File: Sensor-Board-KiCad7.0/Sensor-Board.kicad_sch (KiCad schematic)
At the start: 73 parts, among them J1 B4B-XH-A, U1 OPA396DCKT, U10 BME680, U13 TCA9548AMRGER, U14 OPA396DCKT, U19 MMBFJ177LT1, U2 OPA396DCKT, U20 MMBFJ177LT1, U21 OPA396DCKT, U22 OPA396DCKT, U25 NAU7802SGI, U26 MMBFJ177LT1, U3 OPA396DCKT, U4 NAU7802SGI

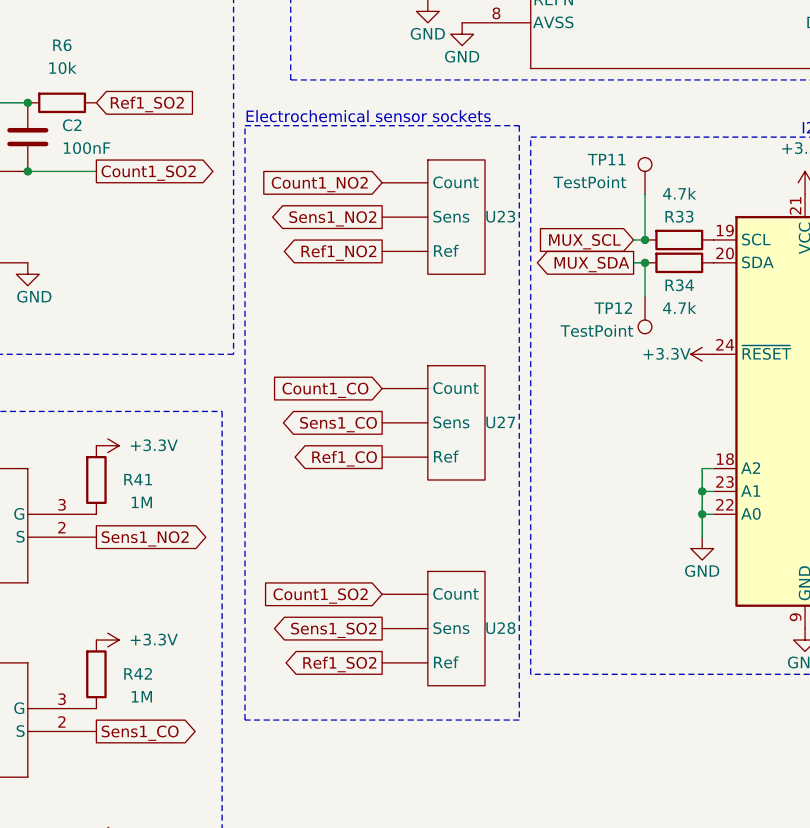
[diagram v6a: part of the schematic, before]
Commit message: Fixed I2C Connector pin numbers
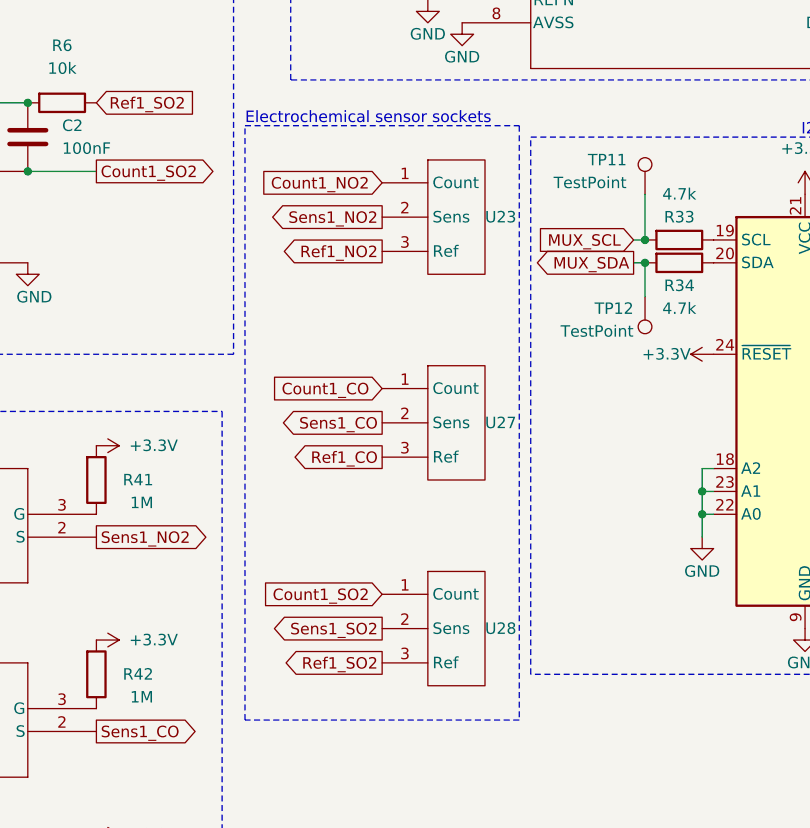
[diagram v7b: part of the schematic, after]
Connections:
- net Count1_CO: now also U27.1 (Count); no longer U27. (Sens)
- net Count1_NO2: now also U23.1 (Count); no longer U23. (Sens)
- net Count1_SO2: now also U28.1 (Count); no longer U28. (Sens)
- net Ref1_CO: now also U27.3 (Ref); no longer U27. (Sens)
- net Ref1_NO2: now also U23.3 (Ref); no longer U23. (Sens)
- net Ref1_SO2: now also U28.3 (Ref); no longer U28. (Sens)
- net Sens1_CO: now also U27.2 (Sens); no longer U27. (Sens)
- net Sens1_NO2: now also U23.2 (Sens); no longer U23. (Sens)
- net Sens1_SO2: now also U28.2 (Sens); no longer U28. (Sens)
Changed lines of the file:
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@@
+    )
+  )
+  (symbol (lib_id "EChem socket:3-pin_socket") (at 198.12 160.02 0) (unit 1)
+    (in_bom yes) (on_board yes) (dnp no)
+    (property "Reference" "U28" (at 204.47 153.67 0)
+      (effects (font (size 1.27 1.27)) (justify left))
+    )
+    (property "Value" "~" (at 198.12 160.02 0)
+      (effects (font (size 1.27 1.27)))
+    )
+    (property "Footprint" "EChem socket:3-pin socket" (at 198.12 160.02 0)
+      (effects (font (size 1.27 1.27)) hide)
+    )
+    (property "Datasheet" "" (at 198.12 160.02 0)
+      (effects (font (size 1.27 1.27)) hide)
+    )
+    (pin "2")
+    (pin "1")
+    (pin "3")
+    (instances
+      (project "Sensor-Board"
+        (path "/3a986dcd-349f-492d-950a-09832b2e5abd"
+          (reference "U28") (unit 1)
+        )
+      )
     )
   )
@@
     )
   )
+  (symbol (lib_id "EChem socket:3-pin_socket") (at 198.12 114.3 0) (unit 1)
+    (in_bom yes) (on_board yes) (dnp no)
+    (property "Reference" "U23" (at 204.47 107.95 0)
+      (effects (font (size 1.27 1.27)) (justify left))
+    )
+    (property "Value" "~" (at 198.12 114.3 0)
+      (effects (font (size 1.27 1.27)))
+    )
+    (property "Footprint" "EChem socket:3-pin socket" (at 198.12 114.3 0)
+      (effects (font (size 1.27 1.27)) hide)
+    )
+    (property "Datasheet" "" (at 198.12 114.3 0)
+      (effects (font (size 1.27 1.27)) hide)
+    )
+    (pin "2")
+    (pin "1")
+    (pin "3")
+    (instances
+      (project "Sensor-Board"
+        (path "/3a986dcd-349f-492d-950a-09832b2e5abd"
+          (reference "U23") (unit 1)
+        )
+      )
+    )
+  )
   (symbol (lib_id "power:+3.3V") (at 40.64 146.05 270) (unit 1)
     (in_bom yes) (on_board yes) (dnp no)
@@
     )
   )
-  (symbol (lib_id "EChem socket:3-pin_socket") (at 198.12 160.02 0) (unit 1)
-    (in_bom yes) (on_board yes) (dnp no)
-    (property "Reference" "U28" (at 204.47 153.67 0)
-      (effects (font (size 1.27 1.27)) (justify left))
-    )
-    (property "Value" "~" (at 198.12 160.02 0)
-      (effects (font (size 1.27 1.27)))
-    )
-    (property "Footprint" "EChem socket:3-pin socket" (at 198.12 160.02 0)
-      (effects (font (size 1.27 1.27)) hide)
-    )
-    (property "Datasheet" "" (at 198.12 160.02 0)
-      (effects (font (size 1.27 1.27)) hide)
-    )
-    (pin "")
-    (pin "")
-    (pin "")
-    (instances
-      (project "Sensor-Board"
-        (path "/3a986dcd-349f-492d-950a-09832b2e5abd"
-          (reference "U28") (unit 1)
-        )
-      )
-    )
-  )
   (symbol (lib_id "power:GND") (at 31.75 189.23 0) (unit 1)
     (in_bom yes) (on_board yes) (dnp no) (fields_autoplaced)
@@
         (path "/3a986dcd-349f-492d-950a-09832b2e5abd"
           (reference "J1") (unit 1)
+        )
+      )
+    )
+  )
+  (symbol (lib_id "EChem socket:3-pin_socket") (at 198.12 137.16 0) (unit 1)
+    (in_bom yes) (on_board yes) (dnp no)
+    (property "Reference" "U27" (at 204.47 130.81 0)
+      (effects (font (size 1.27 1.27)) (justify left))
+    )
+    (property "Value" "~" (at 198.12 137.16 0)
+      (effects (font (size 1.27 1.27)))
+    )
+    (property "Footprint" "EChem socket:3-pin socket" (at 198.12 137.16 0)
+      (effects (font (size 1.27 1.27)) hide)
+    )
+    (property "Datasheet" "" (at 198.12 137.16 0)
+      (effects (font (size 1.27 1.27)) hide)
+    )
+    (pin "2")
+    (pin "1")
+    (pin "3")
+    (instances
+      (project "Sensor-Board"
+        (path "/3a986dcd-349f-492d-950a-09832b2e5abd"
+          (reference "U27") (unit 1)
         )
       )
@@
     )
   )
-  (symbol (lib_id "EChem socket:3-pin_socket") (at 198.12 114.3 0) (unit 1)
-    (in_bom yes) (on_board yes) (dnp no)
-    (property "Reference" "U23" (at 204.47 107.95 0)
-      (effects (font (size 1.27 1.27)) (justify left))
-    )
-    (property "Value" "~" (at 198.12 114.3 0)
-      (effects (font (size 1.27 1.27)))
-    )
-    (property "Footprint" "EChem socket:3-pin socket" (at 198.12 114.3 0)
-      (effects (font (size 1.27 1.27)) hide)
-    )
-    (property "Datasheet" "" (at 198.12 114.3 0)
-      (effects (font (size 1.27 1.27)) hide)
-    )
-    (pin "")
-    (pin "")
-    (pin "")
-    (instances
-      (project "Sensor-Board"
-        (path "/3a986dcd-349f-492d-950a-09832b2e5abd"
-          (reference "U23") (unit 1)
-        )
-      )
-    )
-  )
   (symbol (lib_id "Device:C") (at 153.67 99.06 0) (unit 1)
     (in_bom yes) (on_board yes) (dnp no) (fields_autoplaced)
@@
         )
       )
-    )
-  )
-  (symbol (lib_id "EChem socket:3-pin_socket") (at 198.12 137.16 0) (unit 1)
-    (in_bom yes) (on_board yes) (dnp no)
-    (property "Reference" "U27" (at 204.47 130.81 0)
-      (effects (font (size 1.27 1.27)) (justify left))
-    )
-    (property "Value" "~" (at 198.12 137.16 0)
-      (effects (font (size 1.27 1.27)))
-    )
-    (property "Footprint" "EChem socket:3-pin socket" (at 198.12 137.16 0)
-      (effects (font (size 1.27 1.27)) hide)
-    )
-    (property "Datasheet" "" (at 198.12 137.16 0)
-      (effects (font (size 1.27 1.27)) hide)
-    )
-    (pin "")
-    (pin "")
-    (pin "")
-    (instances
-      (project "Sensor-Board"
-        (path "/3a986dcd-349f-492d-950a-09832b2e5abd"
-          (reference "U27") (unit 1)
-        )
-      )
